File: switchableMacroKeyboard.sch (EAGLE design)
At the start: 36 parts

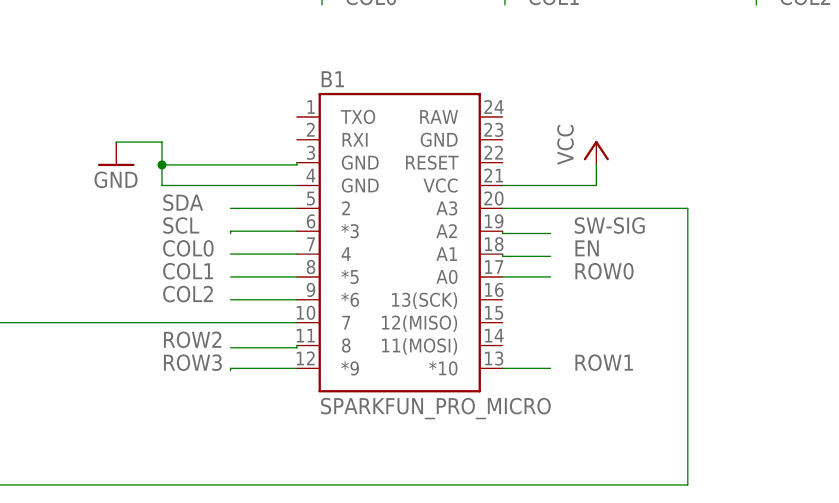
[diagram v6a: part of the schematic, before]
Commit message: Partially rerouted board with several pins moved around on the microcontroller for ease of routing. To do: route columns on bottom layer.
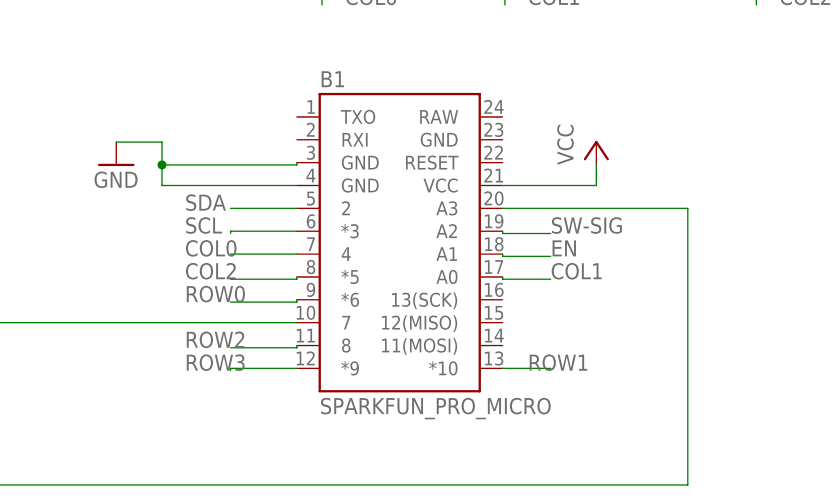
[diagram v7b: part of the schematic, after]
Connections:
- net COL1: now also B1.A0; no longer B1.*5
- net COL2: now also B1.*5; no longer B1.*6
- net ROW0: now also B1.*6; no longer B1.A0
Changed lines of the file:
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@@
 <layer number="115" name="ReferenceISLANDS" color="7" fill="1" visible="no" active="no"/>
 <layer number="116" name="Patch_BOT" color="9" fill="4" visible="yes" active="yes"/>
+<layer number="117" name="PM_Ref" color="7" fill="1" visible="no" active="no"/>
 <layer number="118" name="Rect_Pads" color="7" fill="1" visible="no" active="no"/>
+<layer number="119" name="PF_Ref" color="7" fill="1" visible="no" active="no"/>
+<layer number="120" name="WFL_Ref" color="7" fill="1" visible="no" active="no"/>
 <layer number="121" name="_tsilk" color="7" fill="1" visible="yes" active="yes"/>
 <layer number="122" name="_bsilk" color="7" fill="1" visible="yes" active="yes"/>
@@
 <pinref part="B1" gate="G$1" pin="2"/>
 <wire x1="20.066" y1="-22.606" x2="12.7" y2="-22.606" width="0.1524" layer="91"/>
-<label x="5.08" y="-22.86" size="1.778" layer="95"/>
+<label x="7.62" y="-22.86" size="1.778" layer="95"/>
 </segment>
 <segment>
@@
 <wire x1="42.926" y1="-25.146" x2="42.926" y2="-25.4" width="0.1524" layer="91"/>
 <wire x1="42.926" y1="-25.4" x2="48.26" y2="-25.4" width="0.1524" layer="91"/>
-<label x="50.8" y="-25.4" size="1.778" layer="95"/>
+<label x="48.26" y="-25.4" size="1.778" layer="95"/>
 </segment>
 </net>
@@
 <wire x1="42.926" y1="-27.686" x2="42.926" y2="-27.94" width="0.1524" layer="91"/>
 <wire x1="42.926" y1="-27.94" x2="48.26" y2="-27.94" width="0.1524" layer="91"/>
-<label x="50.8" y="-27.94" size="1.778" layer="95"/>
+<label x="48.26" y="-27.94" size="1.778" layer="95"/>
 </segment>
 <segment>
@@
 </net>
 <net name="ROW0" class="0">
-<segment>
-<pinref part="B1" gate="G$1" pin="A0"/>
-<wire x1="48.26" y1="-30.226" x2="42.926" y2="-30.226" width="0.1524" layer="91"/>
-<label x="50.8" y="-30.48" size="1.778" layer="95"/>
-</segment>
 <segment>
 <pinref part="01" gate="G$1" pin="12"/>
@@
 <label x="-10.16" y="193.04" size="1.778" layer="95"/>
 </segment>
+<segment>
+<pinref part="B1" gate="G$1" pin="*6"/>
+<wire x1="20.066" y1="-32.766" x2="20.066" y2="-33.02" width="0.1524" layer="91"/>
+<wire x1="20.066" y1="-33.02" x2="12.7" y2="-33.02" width="0.1524" layer="91"/>
+<label x="7.62" y="-33.02" size="1.778" layer="95"/>
+</segment>
 </net>
 <net name="ROW3" class="0">
@@
 <wire x1="20.066" y1="-40.386" x2="12.7" y2="-40.386" width="0.1524" layer="91"/>
 <wire x1="12.7" y1="-40.386" x2="12.7" y2="-40.64" width="0.1524" layer="91"/>
-<label x="5.08" y="-40.64" size="1.778" layer="95"/>
+<label x="7.62" y="-40.64" size="1.778" layer="95"/>
 </segment>
 <segment>
@@
 <wire x1="20.066" y1="-37.846" x2="20.066" y2="-38.1" width="0.1524" layer="91"/>
 <wire x1="20.066" y1="-38.1" x2="12.7" y2="-38.1" width="0.1524" layer="91"/>
-<label x="5.08" y="-38.1" size="1.778" layer="95"/>
+<label x="7.62" y="-38.1" size="1.778" layer="95"/>
 </segment>
 <segment>
@@
 <pinref part="B1" gate="G$1" pin="*10"/>
 <wire x1="48.26" y1="-40.386" x2="42.926" y2="-40.386" width="0.1524" layer="91"/>
-<label x="50.8" y="-40.64" size="1.778" layer="95"/>
+<label x="45.72" y="-40.64" size="1.778" layer="95"/>
 </segment>
 </net>
@@
 <wire x1="20.066" y1="-25.146" x2="12.7" y2="-25.146" width="0.1524" layer="91"/>
 <wire x1="12.7" y1="-25.146" x2="12.7" y2="-25.4" width="0.1524" layer="91"/>
-<label x="5.08" y="-25.4" size="1.778" layer="95"/>
+<label x="7.62" y="-25.4" size="1.778" layer="95"/>
 </segment>
 <segment>
@@
 </net>
 <net name="COL2" class="0">
-<segment>
-<pinref part="B1" gate="G$1" pin="*6"/>
-<wire x1="12.7" y1="-32.766" x2="20.066" y2="-32.766" width="0.1524" layer="91"/>
-<label x="5.08" y="-33.02" size="1.778" layer="95"/>
-</segment>
 <segment>
 <pinref part="D12" gate="G$1" pin="C"/>
@@
 <label x="73.66" y="0" size="1.778" layer="95"/>
 </segment>
+<segment>
+<pinref part="B1" gate="G$1" pin="*5"/>
+<wire x1="20.066" y1="-30.226" x2="20.066" y2="-30.48" width="0.1524" layer="91"/>
+<wire x1="20.066" y1="-30.48" x2="12.7" y2="-30.48" width="0.1524" layer="91"/>
+<label x="7.62" y="-30.48" size="1.778" layer="95"/>
+</segment>
 </net>
 <net name="COL1" class="0">
-<segment>
-<pinref part="B1" gate="G$1" pin="*5"/>
-<wire x1="12.7" y1="-30.226" x2="20.066" y2="-30.226" width="0.1524" layer="91"/>
-<label x="5.08" y="-30.48" size="1.778" layer="95"/>
-</segment>
 <segment>
 <pinref part="D8" gate="G$1" pin="C"/>
@@
 <label x="45.72" y="0" size="1.778" layer="95"/>
 </segment>
+<segment>
+<pinref part="B1" gate="G$1" pin="A0"/>
+<wire x1="42.926" y1="-30.226" x2="42.926" y2="-30.48" width="0.1524" layer="91"/>
+<wire x1="42.926" y1="-30.48" x2="48.26" y2="-30.48" width="0.1524" layer="91"/>
+<label x="48.26" y="-30.48" size="1.778" layer="95"/>
+</segment>
 </net>
 <net name="COL0" class="0">
@@
 <pinref part="B1" gate="G$1" pin="4"/>
 <wire x1="12.7" y1="-27.686" x2="20.066" y2="-27.686" width="0.1524" layer="91"/>
-<label x="5.08" y="-27.94" size="1.778" layer="95"/>
-</segment>
-<segment>
+<label x="7.62" y="-27.94" size="1.778" layer="95"/>
+</segment>
+<segment>

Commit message: Added a header file to hold all of the keyboards. Added an LCD test that works.
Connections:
- net ROW0: now also B1.*10; no longer B1.*6
- net ROW1: now also B1.*6; no longer B1.*10
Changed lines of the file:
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@@
 </segment>
 <segment>
-<pinref part="B1" gate="G$1" pin="*6"/>
-<wire x1="20.066" y1="-32.766" x2="20.066" y2="-33.02" width="0.1524" layer="91"/>
-<wire x1="20.066" y1="-33.02" x2="12.7" y2="-33.02" width="0.1524" layer="91"/>
-<label x="7.62" y="-33.02" size="1.778" layer="95"/>
+<pinref part="B1" gate="G$1" pin="*10"/>
+<wire x1="42.926" y1="-40.386" x2="48.26" y2="-40.386" width="0.1524" layer="91"/>
+<wire x1="48.26" y1="-40.386" x2="48.26" y2="-40.64" width="0.1524" layer="91"/>
+<label x="48.26" y="-40.64" size="1.778" layer="95"/>
 </segment>
 </net>
@@
 </segment>
 <segment>
-<pinref part="B1" gate="G$1" pin="*10"/>
-<wire x1="48.26" y1="-40.386" x2="42.926" y2="-40.386" width="0.1524" layer="91"/>
-<label x="45.72" y="-40.64" size="1.778" layer="95"/>
+<pinref part="B1" gate="G$1" pin="*6"/>
+<wire x1="20.066" y1="-32.766" x2="20.066" y2="-33.02" width="0.1524" layer="91"/>
+<wire x1="20.066" y1="-33.02" x2="12.7" y2="-33.02" width="0.1524" layer="91"/>
+<label x="7.62" y="-33.02" size="1.778" layer="95"/>
 </segment>
 </net>
